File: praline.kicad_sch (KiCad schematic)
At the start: 0 parts

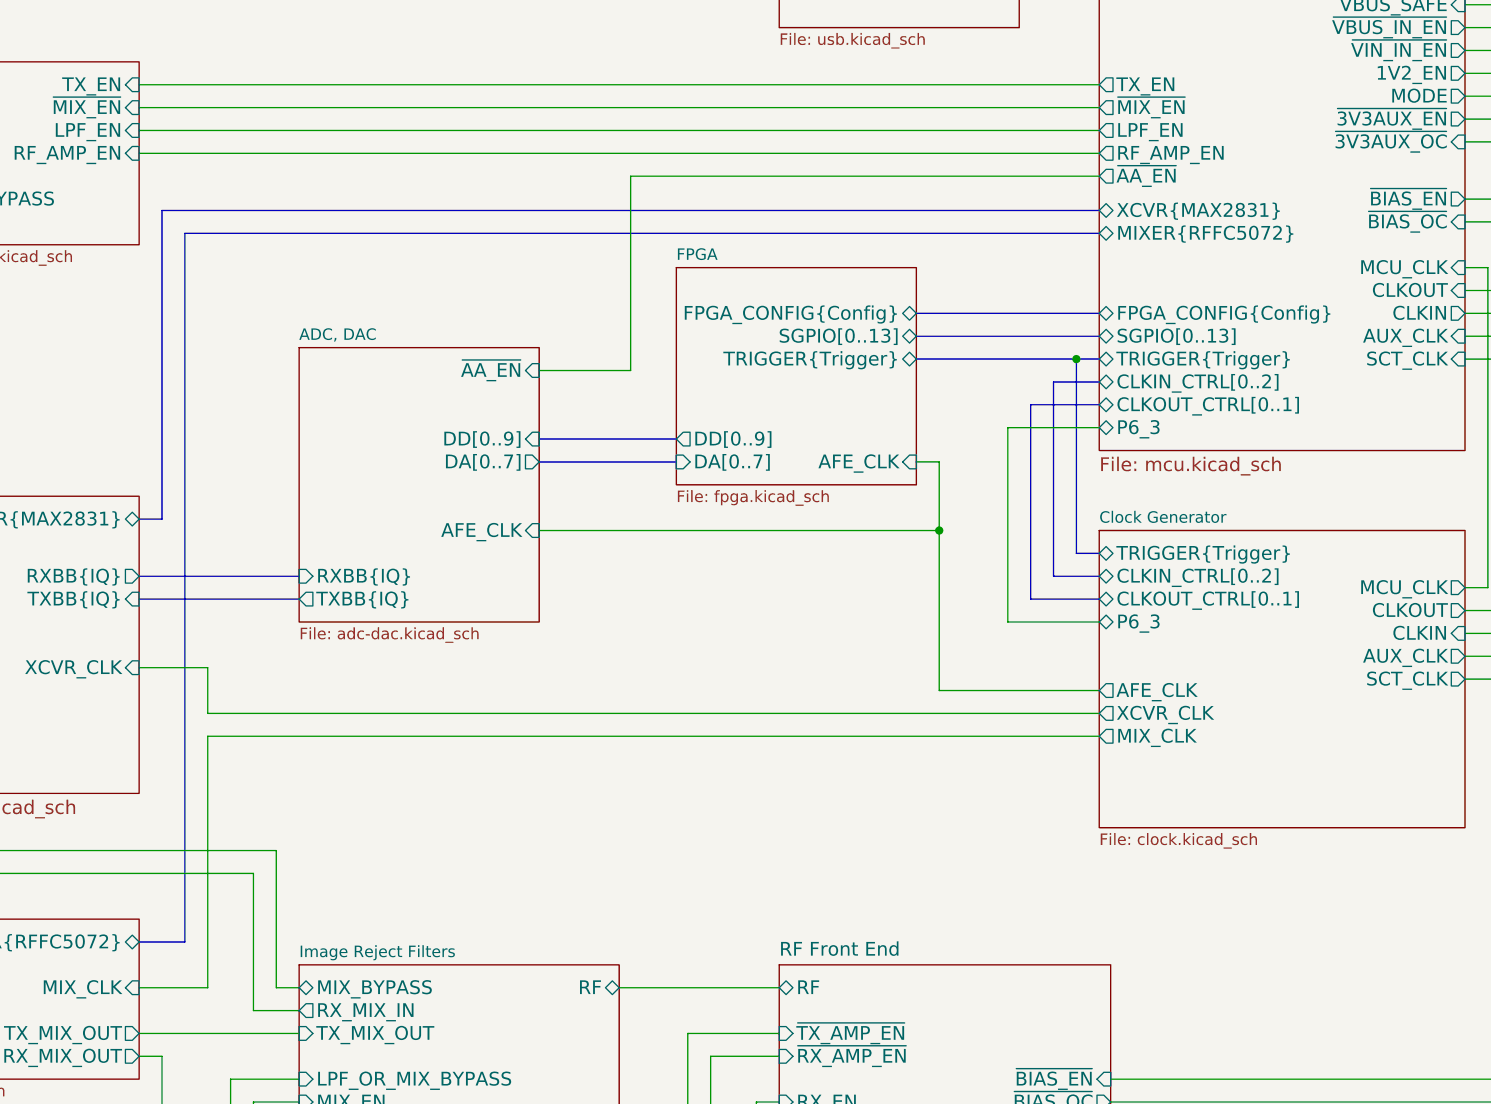
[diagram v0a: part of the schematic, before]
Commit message: Update narrowband anti-aliasing filter
- Add second filter with different bandwidth
- Populate filters
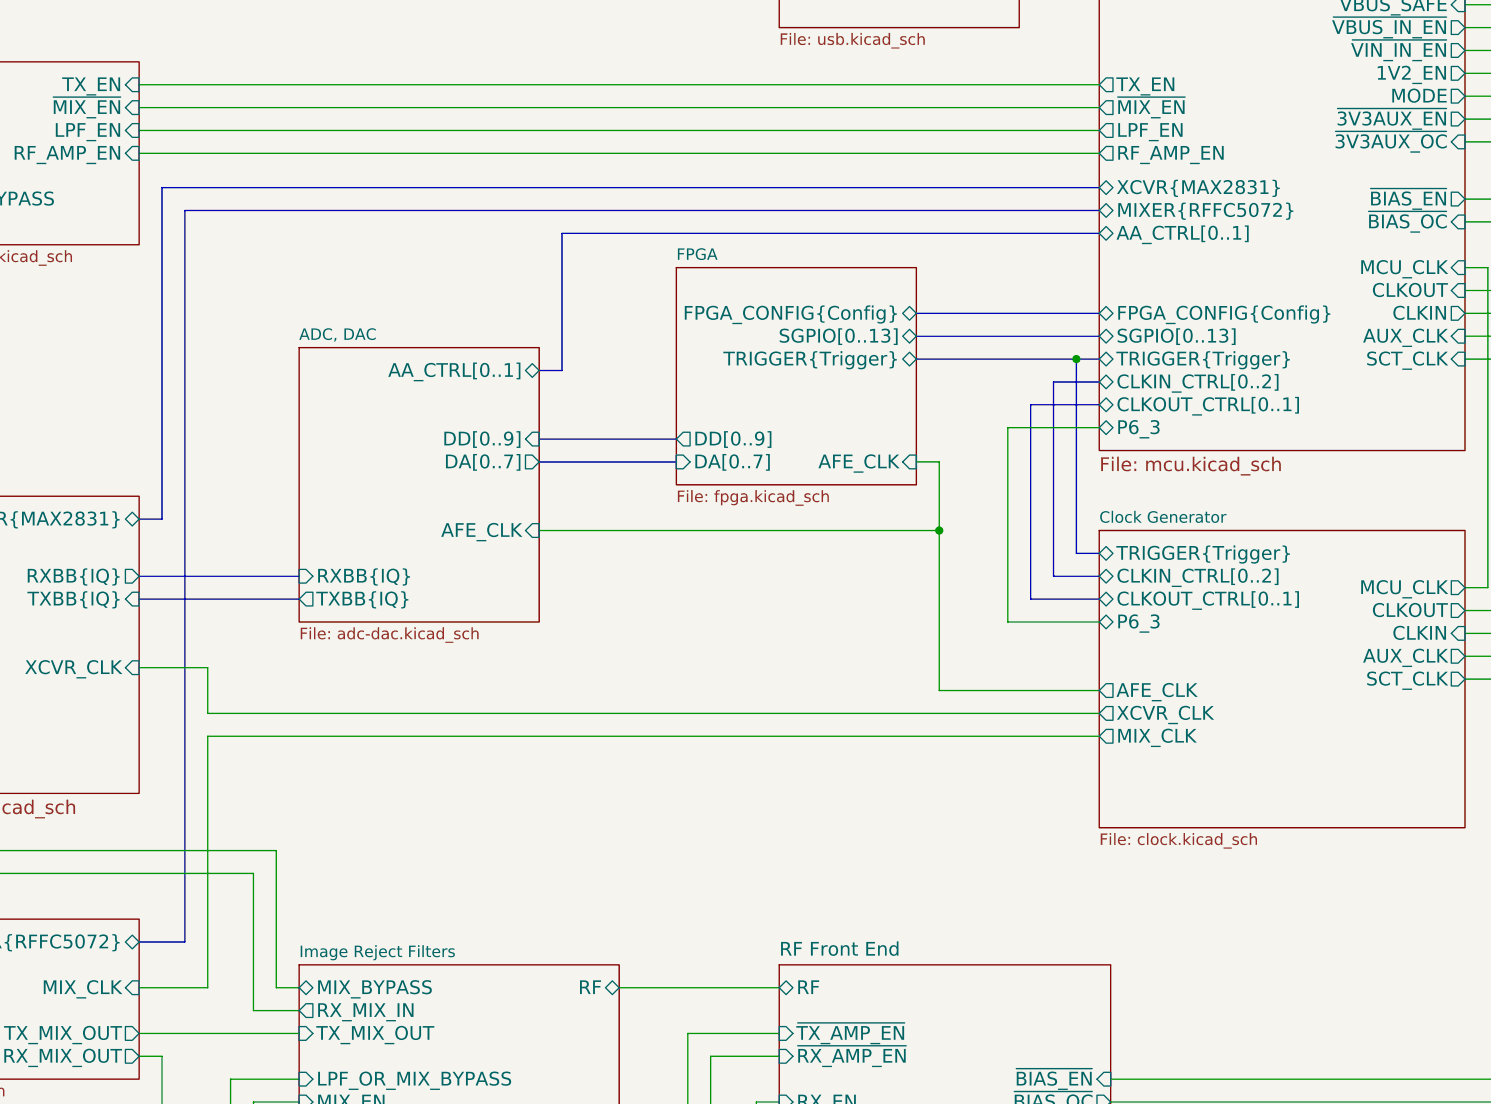
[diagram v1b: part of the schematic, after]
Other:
- sheet ADC, DAC ports: added AA_CTRL[0..1]; removed ~{AA_EN}
- sheet Microcontroller ports: added AA_CTRL[0..1]; removed ~{AA_EN}
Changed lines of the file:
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@@
 	(bus
 		(pts
-			(xy 88.9 58.42) (xy 88.9 92.71)
+			(xy 88.9 55.88) (xy 88.9 92.71)
 		)
 		(stroke
@@
 		)
 	)
-	(wire
-		(pts
-			(xy 140.97 76.2) (xy 130.81 76.2)
-		)
-		(stroke
-			(width 0)
-			(type default)
-		)
-	)
 	(bus
 		(pts
@@
 	(wire
 		(pts
-			(xy 193.04 54.61) (xy 140.97 54.61)
-		)
-		(stroke
-			(width 0)
-			(type default)
-		)
-	)
-	(wire
-		(pts
 			(xy 35.56 170.18) (xy 99.06 170.18)
 		)
@@
 	(wire
 		(pts
-			(xy 140.97 54.61) (xy 140.97 76.2)
-		)
-		(stroke
-			(width 0)
-			(type default)
-		)
-	)
-	(wire
-		(pts
 			(xy 233.68 69.85) (xy 241.3 69.85)
 		)
@@
 	(bus
 		(pts
-			(xy 193.04 58.42) (xy 88.9 58.42)
+			(xy 133.35 60.96) (xy 133.35 76.2)
+		)
+		(stroke
+			(width 0)
+			(type default)
+		)
+	)
+	(bus
+		(pts
+			(xy 193.04 55.88) (xy 88.9 55.88)
 		)
 		(stroke
@@
 		)
 	)
+	(bus
+		(pts
+			(xy 133.35 76.2) (xy 130.81 76.2)
+		)
+		(stroke
+			(width 0)
+			(type default)
+		)
+	)
 	(wire
 		(pts
@@
 	(bus
 		(pts
-			(xy 193.04 60.96) (xy 91.44 60.96)
+			(xy 193.04 58.42) (xy 91.44 58.42)
 		)
 		(stroke
@@
 	(bus
 		(pts
-			(xy 91.44 60.96) (xy 91.44 139.7)
+			(xy 91.44 58.42) (xy 91.44 139.7)
 		)
 		(stroke
@@
 		(pts
 			(xy 50.8 99.06) (xy 50.8 59.69)
+		)
+		(stroke
+			(width 0)
+			(type default)
+		)
+	)
+	(bus
+		(pts
+			(xy 193.04 60.96) (xy 133.35 60.96)
 		)
 		(stroke
@@
 		)
 		(pin "XCVR{MAX2831}" bidirectional
-			(at 193.04 58.42 180)
+			(at 193.04 55.88 180)
 			(effects
 				(font
@@
 			)
 		)
-		(pin "~{AA_EN}" output
-			(at 193.04 54.61 180)
-			(effects
-				(font
-					(size 1.524 1.524)
-				)
-				(justify left)
-			)
-		)
 		(pin "MIXER{RFFC5072}" bidirectional
+			(at 193.04 58.42 180)
+			(effects
+				(font
+					(size 1.524 1.524)
+				)
+				(justify left)
+			)
+		)
+		(pin "AA_CTRL[0..1]" bidirectional
 			(at 193.04 60.96 180)
 			(effects
@@
 			)
 		)
-		(pin "~{AA_EN}" input
+		(pin "AA_CTRL[0..1]" bidirectional
 			(at 130.81 76.2 0)
 			(effects

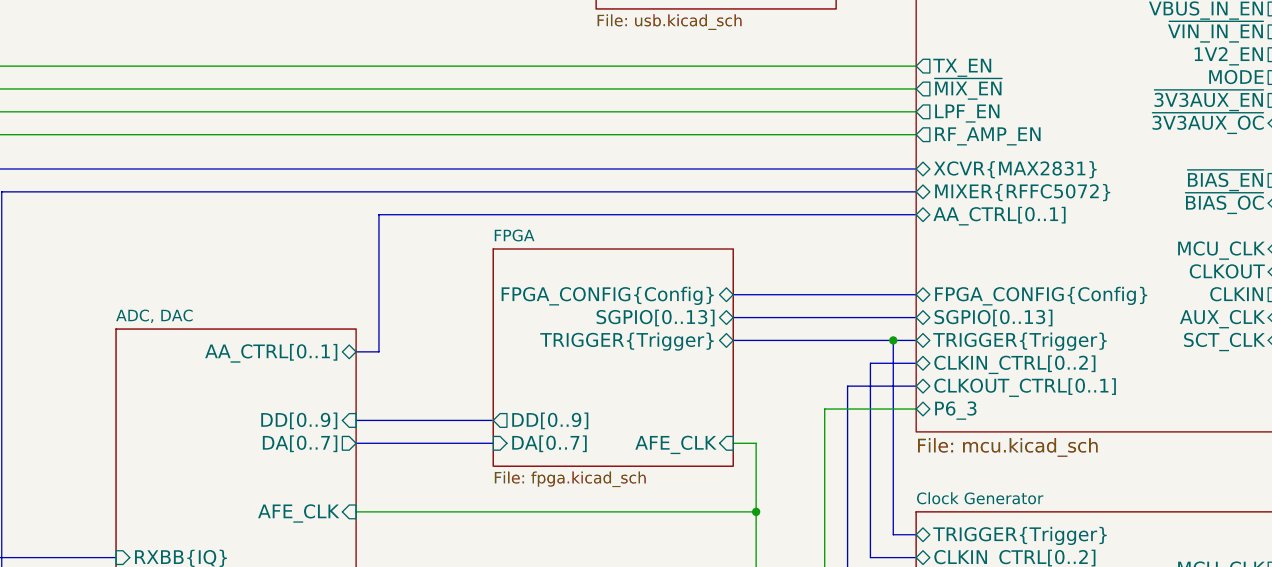
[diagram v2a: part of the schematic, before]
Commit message: Update narrowband anti-aliasing filter
- remove second filter which caused problems
- increase bandwidth of remaining filter
- sharpen filter cut-off
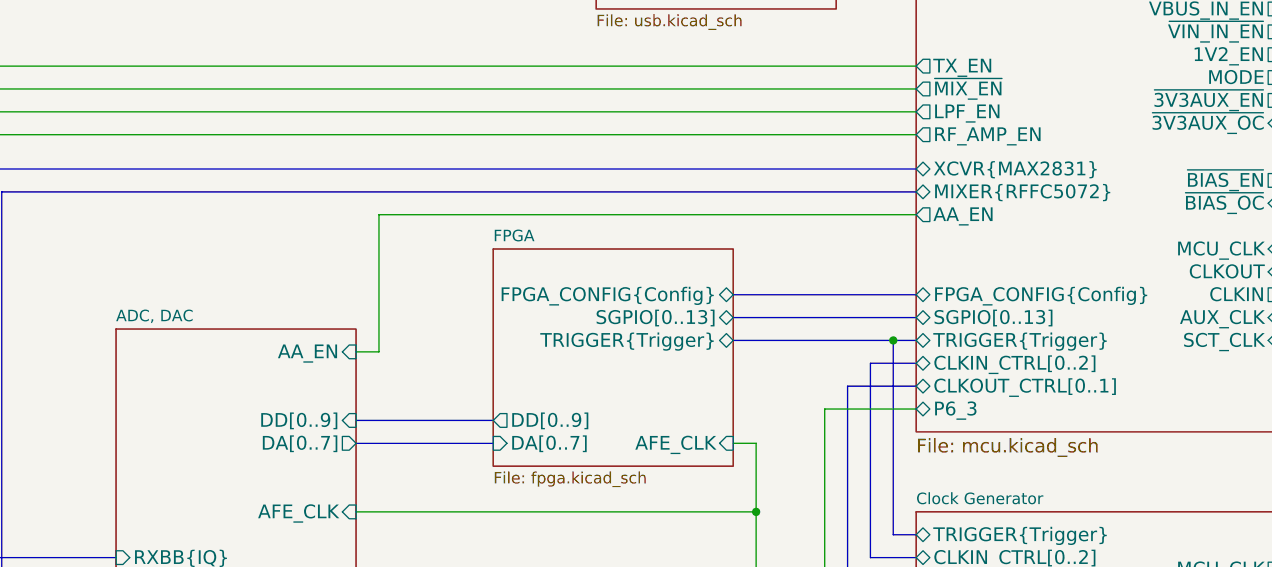
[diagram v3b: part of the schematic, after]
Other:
- sheet ADC, DAC ports: added AA_EN; removed AA_CTRL[0..1]
- sheet Microcontroller ports: added AA_EN; removed AA_CTRL[0..1]
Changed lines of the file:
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@@
-	(bus
-		(pts
-			(xy 133.35 60.96) (xy 133.35 76.2)
-		)
-		(stroke
-			(width 0)
-			(type default)
-		)
-	)
 	(bus
 		(pts
@@
 	(wire
 		(pts
+			(xy 130.81 76.2) (xy 133.35 76.2)
+		)
+		(stroke
+			(width 0)
+			(type default)
+		)
+	)
+	(wire
+		(pts
 			(xy 48.26 152.4) (xy 53.34 152.4)
 		)
@@
 		)
 	)
-	(bus
-		(pts
-			(xy 133.35 76.2) (xy 130.81 76.2)
-		)
-		(stroke
-			(width 0)
-			(type default)
-		)
-	)
 	(wire
 		(pts
@@
 	(wire
 		(pts
+			(xy 133.35 60.96) (xy 193.04 60.96)
+		)
+		(stroke
+			(width 0)
+			(type default)
+		)
+	)
+	(wire
+		(pts
 			(xy 101.6 177.8) (xy 101.6 160.02)
 		)
@@
 	(wire
 		(pts
+			(xy 133.35 76.2) (xy 133.35 60.96)
+		)
+		(stroke
+			(width 0)
+			(type default)
+		)
+	)
+	(wire
+		(pts
 			(xy 193.04 82.55) (xy 182.88 82.55)
 		)
@@
 		(pts
 			(xy 50.8 99.06) (xy 50.8 59.69)
-		)
-		(stroke
-			(width 0)
-			(type default)
-		)
-	)
-	(bus
-		(pts
-			(xy 193.04 60.96) (xy 133.35 60.96)
 		)
 		(stroke
@@
 			)
 		)
-		(pin "AA_CTRL[0..1]" bidirectional
+		(pin "AA_EN" output
 			(at 193.04 60.96 180)
 			(effects
@@
 			)
 		)
-		(pin "AA_CTRL[0..1]" bidirectional
+		(pin "AA_EN" input
 			(at 130.81 76.2 0)
 			(effects
